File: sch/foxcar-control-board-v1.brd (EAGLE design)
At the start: 178 x 95.4 mm, 91 parts, among them U1 HMC5883LSMD, U2 SPX29300

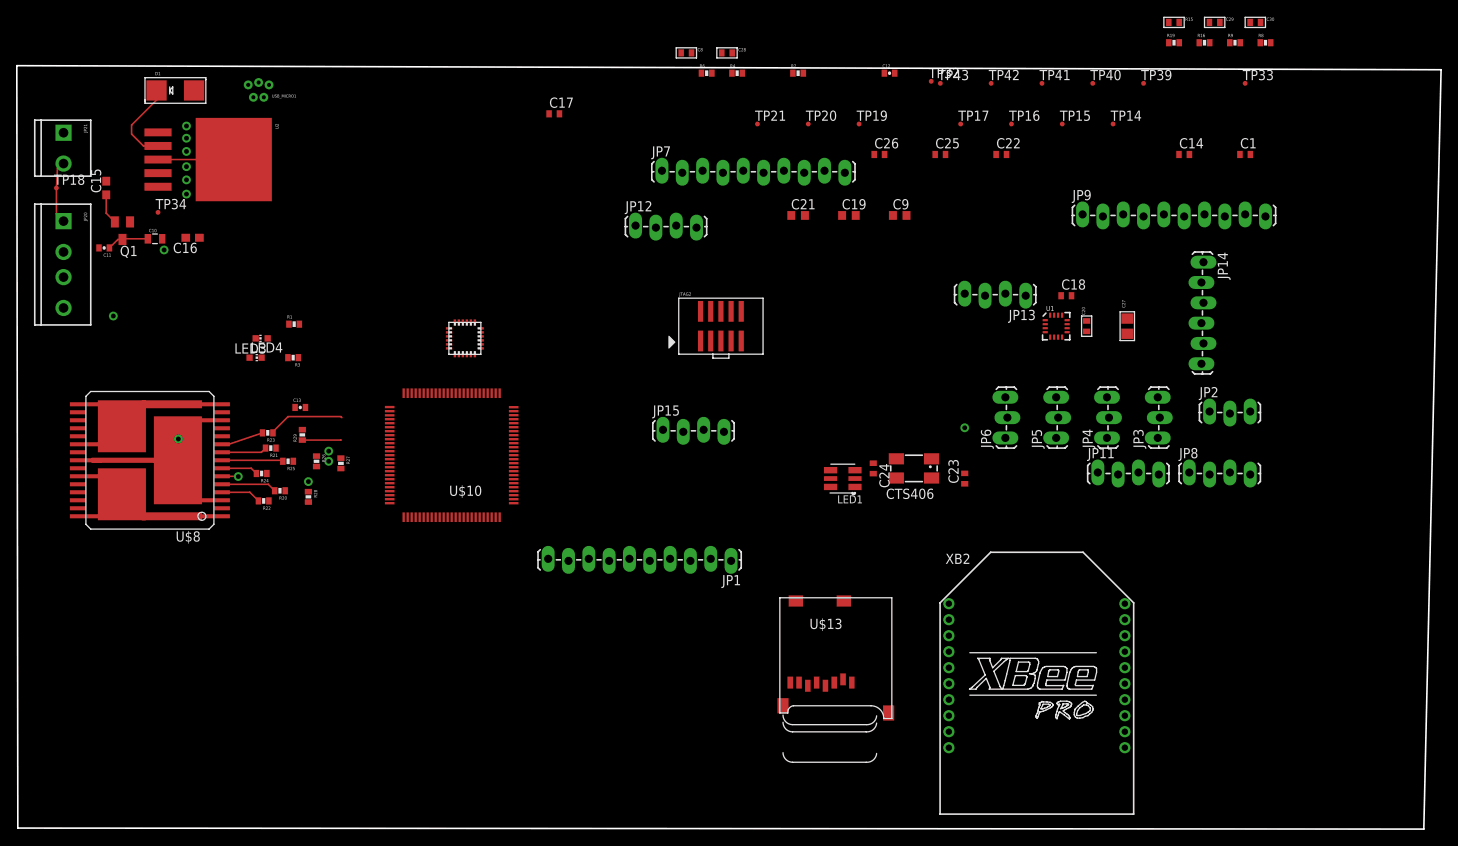
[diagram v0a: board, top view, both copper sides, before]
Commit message: Almost done with power layout. Minor stm32 symbol changes.
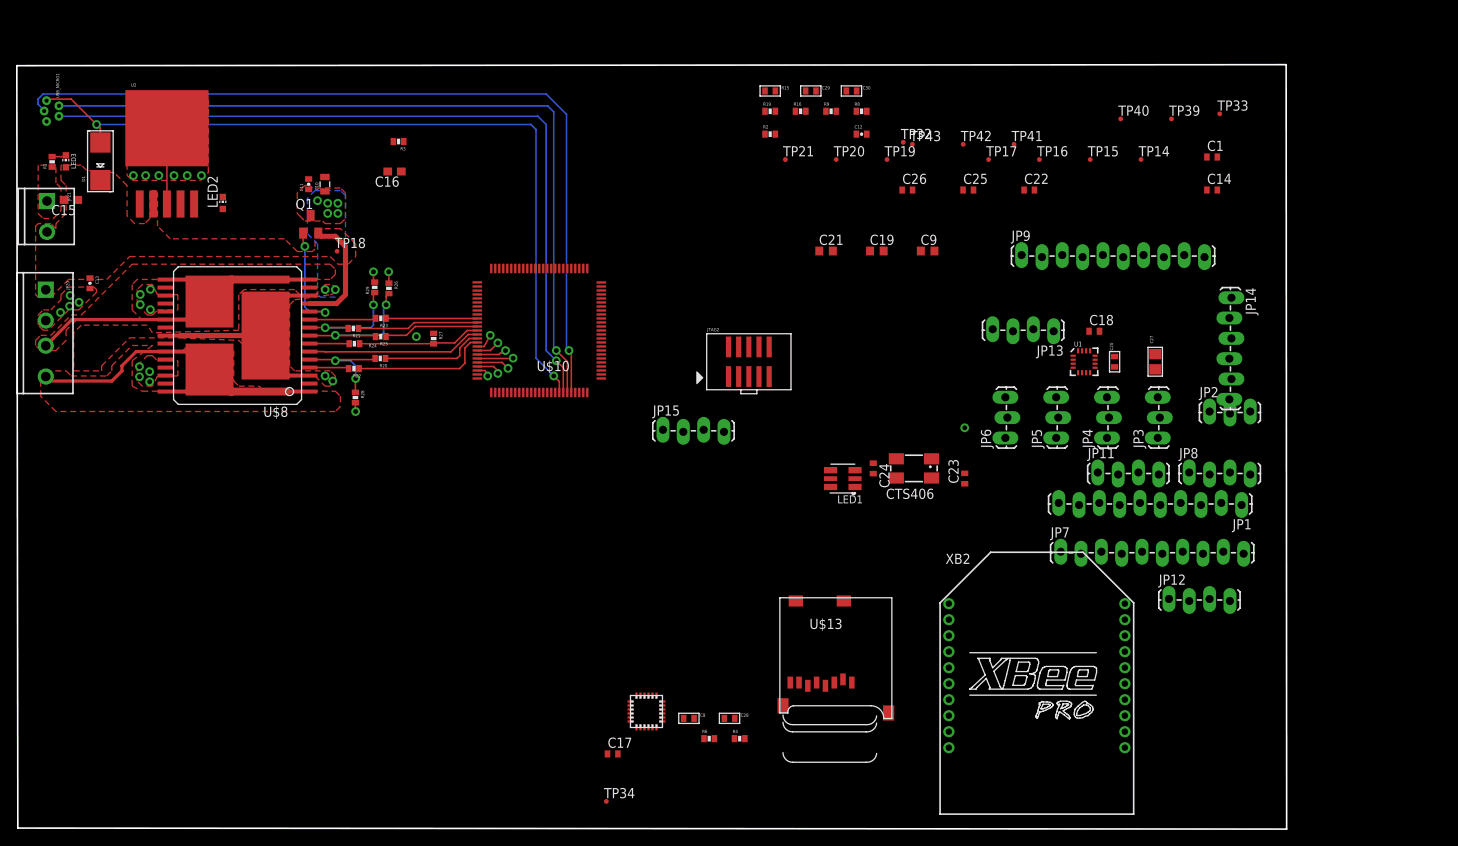
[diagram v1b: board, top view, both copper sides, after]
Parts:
- removed LED4: GREEN, led:CHIP-LED0603
- added LED2: GREEN, led:CHIP-LED0603
- moved TP34 92.5 mm to (73.6, 3.33)
- moved C28 83.2 mm to (89.0, 13.7)
- moved C8 83.2 mm to (83.9, 13.7)
- moved R4 83.2 mm to (90.2, 11.2)
- moved R6 83.2 mm to (86.4, 11.2)
- moved JP12 81.4 mm to (143.9, 28.6)
- moved C17 80.3 mm to (74.4, 9.27)
- moved JP7 68.9 mm to (130.4, 34.4)
- moved JP1 64.2 mm to (153.0, 40.5)
- moved U$3 51.9 mm to (78.6, 14.6)
- moved R15 51.2 mm to (94.0, 92.1)
- moved R16 51.2 mm to (97.9, 89.6)
- moved R19 51.2 mm to (94.0, 89.6)
- moved C30 51.2 mm to (104.2, 92.1)
- moved C29 51.2 mm to (99.1, 92.1)
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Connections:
- net N$76 renamed INB
- net N$77 renamed CP
- net N$78 renamed VCC
- net N$79 renamed INA
- net N$83 renamed ENB
- net N$84 renamed ENA
- net N$85 renamed PWM
- net N$86 renamed CS
- removed net N$80: JP20.3, U$8.1, U$8.25, U$8.30, U$8.OUTA, U$8.OUTA@1
- removed net N$81: JP20.4, U$8.15, U$8.16, U$8.21, U$8.OUTB, U$8.OUTB@1
- new net OUTA: JP20.4, U$8.1, U$8.25, U$8.30, U$8.OUTA, U$8.OUTA@1
- new net OUTB: JP20.3, U$8.15, U$8.16, U$8.21, U$8.OUTB, U$8.OUTB@1
- net 3.3V: now also LED2.A; no longer LED4.A
- net MD_CS: now also U$10.PB2; no longer U$10.PB1
- net MD_CSDIS: now also U$10.PE8; no longer U$10.PB0
- net MD_ENA: now also U$10.PE9; no longer U$10.PE10
- net MD_ENB: now also U$10.PB1; no longer U$10.PE9
- net MD_INA: now also U$10.PE10; no longer U$10.PE8
- net MD_INB: now also U$10.PB0; no longer U$10.PE7
- net MD_PWM: now also U$10.PE7; no longer U$10.PB2
- net N$2: now also LED2.C; no longer LED4.C
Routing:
- net FS_DP: track 0.00 -> 104.2 mm, vias 0 -> 1
- net FS_VBUS: track 0.00 -> 99.4 mm, vias 0 -> 2
- net FS_DM: track 0.00 -> 97.9 mm, vias 0 -> 1
- net FS_ID: track 0.00 -> 95.7 mm, vias 0 -> 1
- net OUTB: track 0.00 -> 33.7 mm
- net OUTA: track 0.00 -> 21.1 mm
- net MD_CSDIS: track 2.05 -> 21.9 mm, vias 1 -> 0
- net MD_INA: track 0.00 -> 17.2 mm
- net MD_PWM: track 0.00 -> 15.4 mm
- net MD_ENB: track 0.00 -> 15.2 mm
- net CP: track 0.00 -> 14.1 mm, vias 0 -> 2
- net MD_ENA: track 0.00 -> 13.1 mm
- net CS: track 7.67 -> 19.7 mm, vias 0 -> 2
- net MD_CS: track 0.00 -> 11.9 mm
- net ENA: track 6.94 -> 14.5 mm, vias 0 -> 2
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- added copper zone on layer 15, net 3.3V
- added copper zone on layer 1, net GND
- added copper zone on layer 1, net OUTA
- added copper zone on layer 1, net OUTB
- added copper zone on layer 1, net VCC
- added copper zone on layer 16, net VCC
- added copper zone on layer 1, net VIN
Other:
- board size 178 x 95.4 mm -> 158.7 x 95.6 mm

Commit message: Making progress on layout.
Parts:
- R15: device microbuilder:0402 -> SparkFun-Passives:0402-RES
- moved JP2 145.1 mm to (4.51, 38.1)
- moved JP5 110.2 mm to (20.1, 38.0), turned to 180 degrees
- moved TP15 106.5 mm to (36.6, 40.7)
- moved JP4 105.4 mm to (31.2, 38.0), turned to 180 degrees
- moved TP14 103.3 mm to (46.4, 40.7)
- moved JP14 102.4 mm to (49.3, 66.4), turned to 90 degrees
- moved JP13 99.1 mm to (31.7, 46.2)
- moved TP21 98.3 mm to (7.68, 40.4)
- moved TP20 96.7 mm to (15.6, 40.7)
- moved C1 95.4 mm to (55.0, 69.2), turned to 270 degrees
- moved TP19 93.0 mm to (26.1, 40.7)
- moved JP9 92.8 mm to (34.4, 89.3)
- moved R16 92.0 mm to (7.68, 71.2)
- moved JP3 91.5 mm to (51.6, 38.4), turned to 180 degrees
- moved TP16 88.7 mm to (78.8, 9.59)
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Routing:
- net FS_DP: track 104.2 -> 5.81 mm
- net FS_DM: track 97.9 -> 0.00 mm, vias 1 -> 0
- net FS_VBUS: track 99.4 -> 2.35 mm, vias 2 -> 1
- net FS_ID: track 95.7 -> 0.00 mm, vias 1 -> 0
- net DIR: track 2.45 -> 74.2 mm
- net ESCD: track 2.97 -> 60.1 mm
- net 3.3V: track 2.46 -> 36.2 mm, vias 3 -> 14
- net GND: track 10.9 -> 28.7 mm, vias 20 -> 36
- net SPI1_NSS: track 0.00 -> 15.3 mm
- net SPI1_SCK: track 0.00 -> 13.0 mm
- net SPI1_MISO: track 0.00 -> 11.3 mm
- net TX2: track 0.00 -> 11.0 mm
- net RX2: track 0.00 -> 11.0 mm
- net SPI1_MOSI: track 0.00 -> 9.46 mm
- net ESCB: track 4.48 -> 11.3 mm
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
